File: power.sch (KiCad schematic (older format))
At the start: 46 parts, among them J2 BATT_OUT, J3 BATT_IN, J4 Barrel_Jack_Switch, K1 UMS05-1A80-75L, Q2 Q_NMOS_DSG, SW2 SW_Reed, U1 TPS62821DLC, U4 TPS62821DLC, U5 P783F-Q24-S5-S

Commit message: Small fixes to schematic.
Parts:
- added R?: 39k, symbol Device:R_US
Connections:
- wire segments 132 -> 133
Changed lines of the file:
@@
 RELAY-
 Wire Wire Line
-	2000 5250 1200 5250
-Wire Wire Line
 	1200 5250 1200 5450
-Connection ~ 2000 5250
 $Comp
 L Device:R_US R10
@@
 Wire Wire Line
 	1200 5250 1050 5250
-Connection ~ 1200 5250
 Wire Notes Line width 20
 	550  4000 3200 4000
@@
 $EndComp
 NoConn ~ 8400 1050
+$Comp
+L Device:R_US R?
+U 1 1 618DE97F
+P 1550 5250
+F 0 "R?" V 1345 5250 50  0000 C CNN
+F 1 "39k" V 1436 5250 50  0000 C CNN
+F 2 "" V 1590 5240 50  0001 C CNN
+F 3 "~" H 1550 5250 50  0001 C CNN
+	1    1550 5250
+	0    1    1    0
+$EndComp
+Wire Wire Line
+	1200 5250 1400 5250
+Connection ~ 1200 5250
+Wire Wire Line
+	1700 5250 2000 5250
+Connection ~ 2000 5250
 $EndSCHEMATC

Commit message: Updated footprints. Placed components and added silkscreen.
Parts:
- removed C26: 0.47u, Capacitor_SMD:C_1206_3216Metric, symbol Device:C
- removed C27, C28: 4.7u, Capacitor_SMD:C_1206_3216Metric, symbol Device:C
- removed C30, C31, C33, C34: 10u, Capacitor_SMD:C_1206_3216Metric, symbol Device:C
- removed L1, L2: 0.47u, Inductor_SMD:L_0603_1608Metric, symbol Device:L
- removed R15: 30k, Resistor_SMD:R_0603_1608Metric, symbol Device:R_US
- removed R16: 20k, Resistor_SMD:R_0603_1608Metric, symbol Device:R_US
- removed R17: 50k, Resistor_SMD:R_0603_1608Metric, symbol Device:R_US
- removed R19: 470k, Resistor_SMD:R_0603_1608Metric, symbol Device:R_US
- removed R20, R22: 100k, Resistor_SMD:R_0603_1608Metric, symbol Device:R_US
- removed R21: 82k, Resistor_SMD:R_0603_1608Metric, symbol Device:R_US
- removed TP10: 3.3v, TestPoint:TestPoint_Pad_1.5x1.5mm, symbol Connector:TestPoint
- removed TP6: 1.1v EN, TestPoint:TestPoint_Pad_1.5x1.5mm, symbol Connector:TestPoint
- removed TP7: 3.3v EN, TestPoint:TestPoint_Pad_1.5x1.5mm, symbol Connector:TestPoint
- removed TP8: 1.1v, TestPoint:TestPoint_Pad_1.5x1.5mm, symbol Connector:TestPoint
- removed U1, U4: TPS62821DLC, Package_DFN_QFN:Texas_VSON-HR-8_1.5x2mm_P0.5mm, symbol Regulator_Switching:TPS62821DLC
- added J11: Screw_Terminal_01x02, TerminalBlock:TerminalBlock_bornier-2_P5.08mm, symbol Connector:Screw_Terminal_01x02
- D2, D3: footprint Diode_SMD:D_0603_1608Metric -> Diode_SMD:D_1206_3216Metric_Pad1.42x1.75mm_HandSolder
- J2: footprint TerminalBlock:TerminalBlock_Altech_AK300-2_P5.00mm -> TerminalBlock:TerminalBlock_bornier-2_P5.08mm
- R1: renamed from R?; footprint (none) -> Resistor_SMD:R_1206_3216Metric_Pad1.30x1.75mm_HandSolder
- R10, R11, R12, R13, R14, R18: footprint Resistor_SMD:R_0603_1608Metric -> Resistor_SMD:R_1206_3216Metric_Pad1.30x1.75mm_HandSolder
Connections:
- net labels removed: +1V1, +3V3
- wire segments 133 -> 70
- no-connect marks 2 -> 1
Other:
- note removed: "RC Filter delays enable by 9.5ms"
- moved on the sheet: C29, C32, D4, D5, F1, J2, J3, J4, K1, R14, R18, TP9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

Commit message: Changed footprints to right angle versions. Adjusted board outline to orbitty carrier size.
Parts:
- J3: footprint Connector_AMASS:AMASS_XT30U-F_1x02_P5.0mm_Vertical -> Connector_AMASS:AMASS_XT30PW-M_1x02_P2.50mm_Horizontal
- SW2: footprint Connector_JST:JST_PH_B2B-PH-K_1x02_P2.00mm_Vertical -> Connector_JST:JST_PH_S2B-PH-K_1x02_P2.00mm_Horizontal
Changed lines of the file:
@@
 F 0 "SW2" V 2046 4965 50  0000 R CNN
 F 1 "SW_Reed" V 1955 4965 50  0000 R CNN
-F 2 "Connector_JST:JST_PH_B2B-PH-K_1x02_P2.00mm_Vertical" H 2000 5050 50  0001 C CNN
+F 2 "Connector_JST:JST_PH_S2B-PH-K_1x02_P2.00mm_Horizontal" H 2000 5050 50  0001 C CNN
 F 3 "~" H 2000 5050 50  0001 C CNN
 	1    2000 5050
@@
 F 0 "J3" H 1180 2242 50  0000 L CNN
 F 1 "BATT_IN" H 1180 2151 50  0000 L CNN
-F 2 "Connector_AMASS:AMASS_XT30U-F_1x02_P5.0mm_Vertical" H 1100 2250 50  0001 C CNN
+F 2 "Connector_AMASS:AMASS_XT30PW-M_1x02_P2.50mm_Horizontal" H 1100 2250 50  0001 C CNN
 F 3 "~" H 1100 2250 50  0001 C CNN
 	1    1100 2250

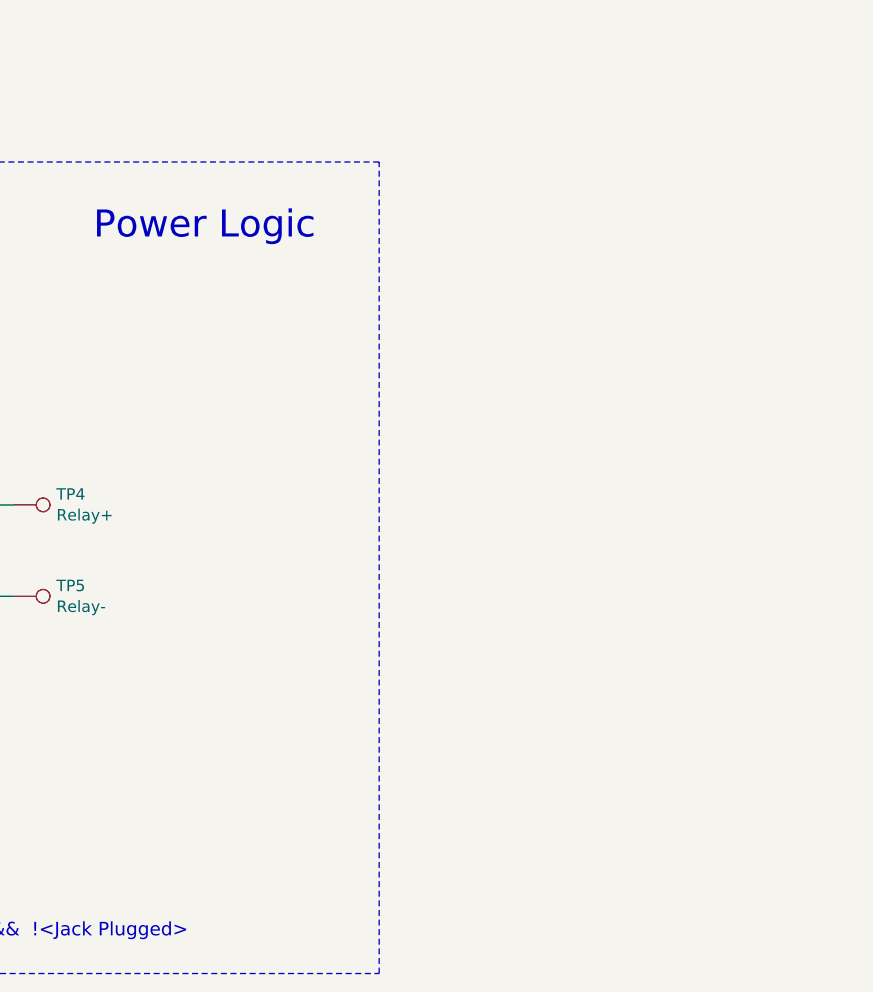
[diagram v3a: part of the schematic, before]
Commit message: Added battery undervoltage protection, needs consideration as to whether it would work.
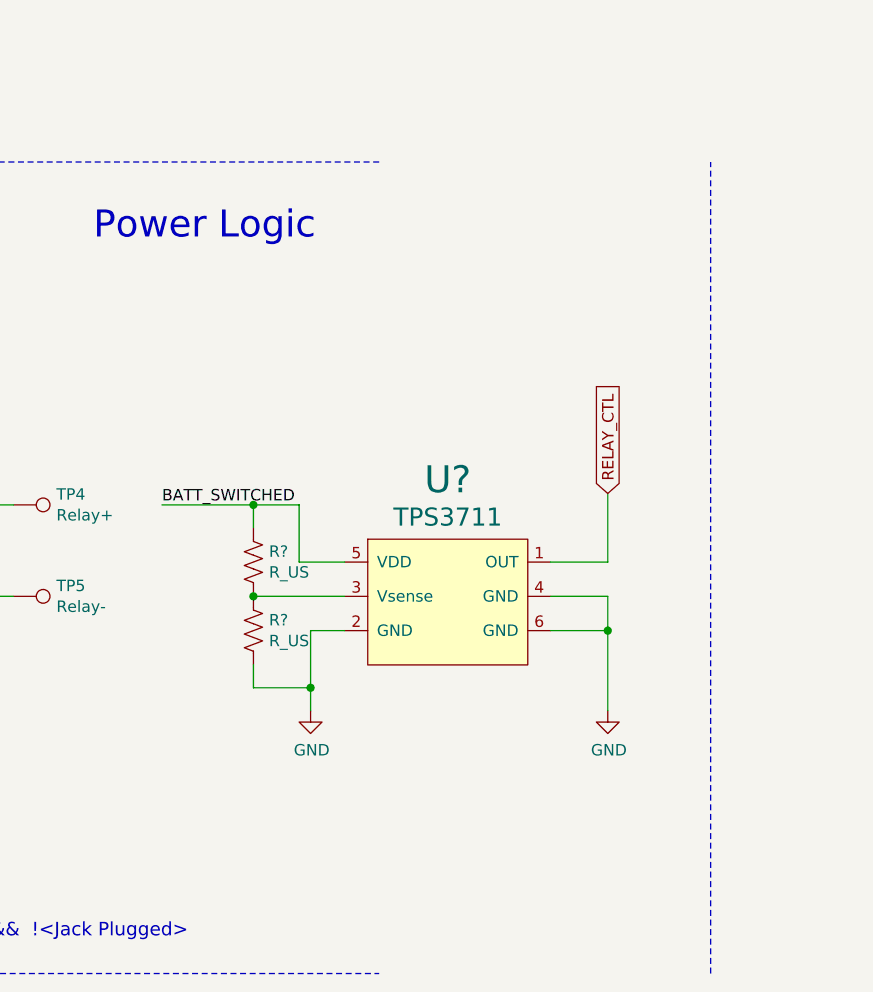
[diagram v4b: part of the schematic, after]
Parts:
- added R? (x2): R_US, symbol Device:R_US
- added U?: TPS3711, symbol New_Library:TPS3711
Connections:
- net BATT_SWITCHED: now also R?.1, U?.5 (VDD)
- net GND: now also R?.2, U?.2 (GND), U?.4 (GND), U?.6 (GND)
- net RELAY_CTL: now also U?.1 (OUT)
- new net: R?.1, R?.2, U?.3 (Vsense)
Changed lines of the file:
@@
 	550  7700 5400 7700
 Wire Notes Line width 20
-	5400 7700 5400 4150
+	6850 7700 6850 4150
 Wire Notes Line width 20
 	5400 4150 550  4150
@@
 	1    0    0    -1
 $EndComp
+$Comp
+L New_Library:TPS3711 U?
+U 1 1 618E2051
+P 5700 6200
+F 0 "U?" H 5700 6860 118 0000 C CNN
+F 1 "TPS3711" H 5700 6696 79  0000 C CNN
+F 2 "" H 5700 6700 118 0001 C CNN
+F 3 "" H 5700 6700 118 0001 C CNN
+	1    5700 6200
+	1    0    0    -1
+$EndComp
+$Comp
+L power:GND #PWR?
+U 1 1 618E412F
+P 6400 6550
+F 0 "#PWR?" H 6400 6300 50  0001 C CNN
+F 1 "GND" H 6405 6377 50  0000 C CNN
+F 2 "" H 6400 6550 50  0001 C CNN
+F 3 "" H 6400 6550 50  0001 C CNN
+	1    6400 6550
+	1    0    0    -1
+$EndComp
+Wire Wire Line
+	6150 6050 6400 6050
+Wire Wire Line
+	6400 6050 6400 6200
+Wire Wire Line
+	6150 6200 6400 6200
+Connection ~ 6400 6200
+Wire Wire Line
+	6400 6200 6400 6550
+Wire Wire Line
+	5250 6200 5100 6200
+Wire Wire Line
+	5100 6200 5100 6450
+$Comp
+L power:GND #PWR?
+U 1 1 618EA162
+P 5100 6550
+F 0 "#PWR?" H 5100 6300 50  0001 C CNN
+F 1 "GND" H 5105 6377 50  0000 C CNN
+F 2 "" H 5100 6550 50  0001 C CNN
+F 3 "" H 5100 6550 50  0001 C CNN
+	1    5100 6550
+	1    0    0    -1
+$EndComp
+Wire Wire Line
+	6150 5900 6400 5900
+Wire Wire Line
+	6400 5900 6400 5600
+Text GLabel 6400 5600 1    50   Input ~ 0
+RELAY_CTL
+Wire Wire Line
+	5250 5900 5050 5900
+Wire Wire Line
+	5050 5900 5050 5650
+Wire Wire Line
+	5250 6050 4850 6050
+$Comp
+L Device:R_US R?
+U 1 1 618F8E38
+P 4850 5900
+F 0 "R?" H 4918 5946 50  0000 L CNN
+F 1 "R_US" H 4918 5855 50  0000 L CNN
+F 2 "" V 4890 5890 50  0001 C CNN
+F 3 "~" H 4850 5900 50  0001 C CNN
+	1    4850 5900
+	1    0    0    -1
+$EndComp
+$Comp
+L Device:R_US R?
+U 1 1 618F9768
+P 4850 6200
+F 0 "R?" H 4918 6246 50  0000 L CNN
+F 1 "R_US" H 4918 6155 50  0000 L CNN
+F 2 "" V 4890 6190 50  0001 C CNN
+F 3 "~" H 4850 6200 50  0001 C CNN
+	1    4850 6200
+	1    0    0    -1
+$EndComp
+Connection ~ 4850 6050
+Wire Wire Line
+	4850 6350 4850 6450
+Wire Wire Line
+	4850 6450 5100 6450
+Connection ~ 5100 6450
+Wire Wire Line
+	5100 6450 5100 6550
+Wire Wire Line
+	4850 5750 4850 5650
+Wire Wire Line
+	4850 5650 5050 5650
+Wire Wire Line
+	4850 5650 4450 5650
+Connection ~ 4850 5650
+Text Label 4450 5650 0    50   ~ 0
+BATT_SWITCHED
 $EndSCHEMATC

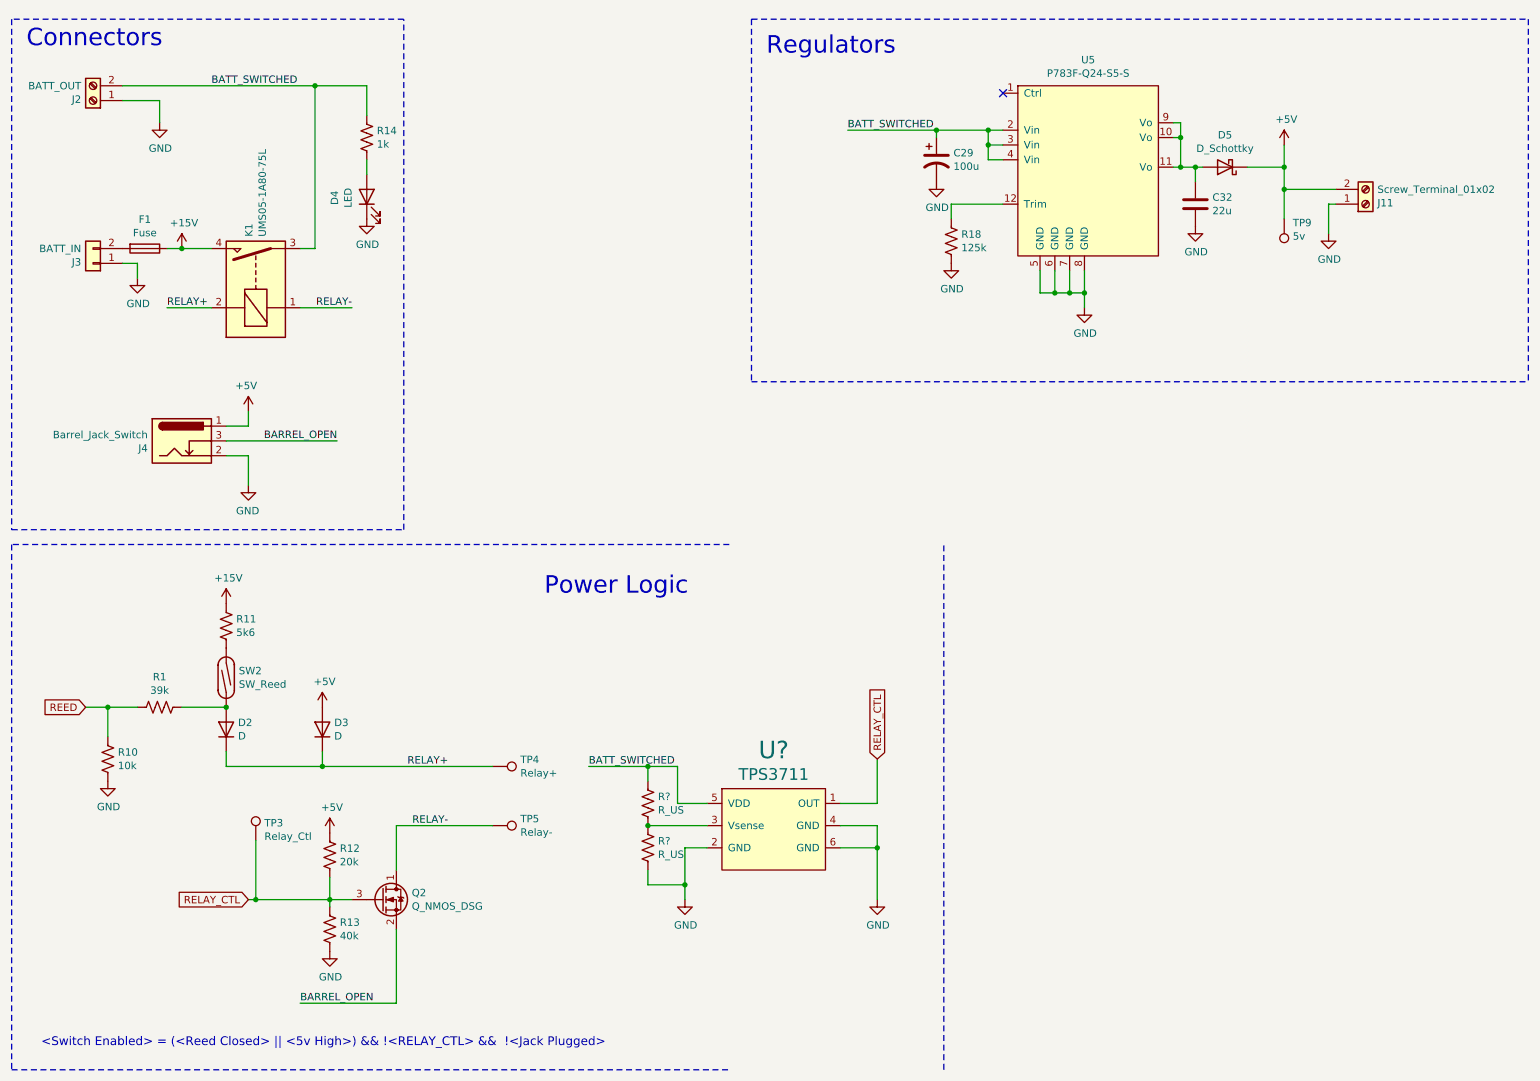
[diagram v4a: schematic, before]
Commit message: Removed uneeded DC barrel power. Adjusted component values for 12v supply. Checked footprints.
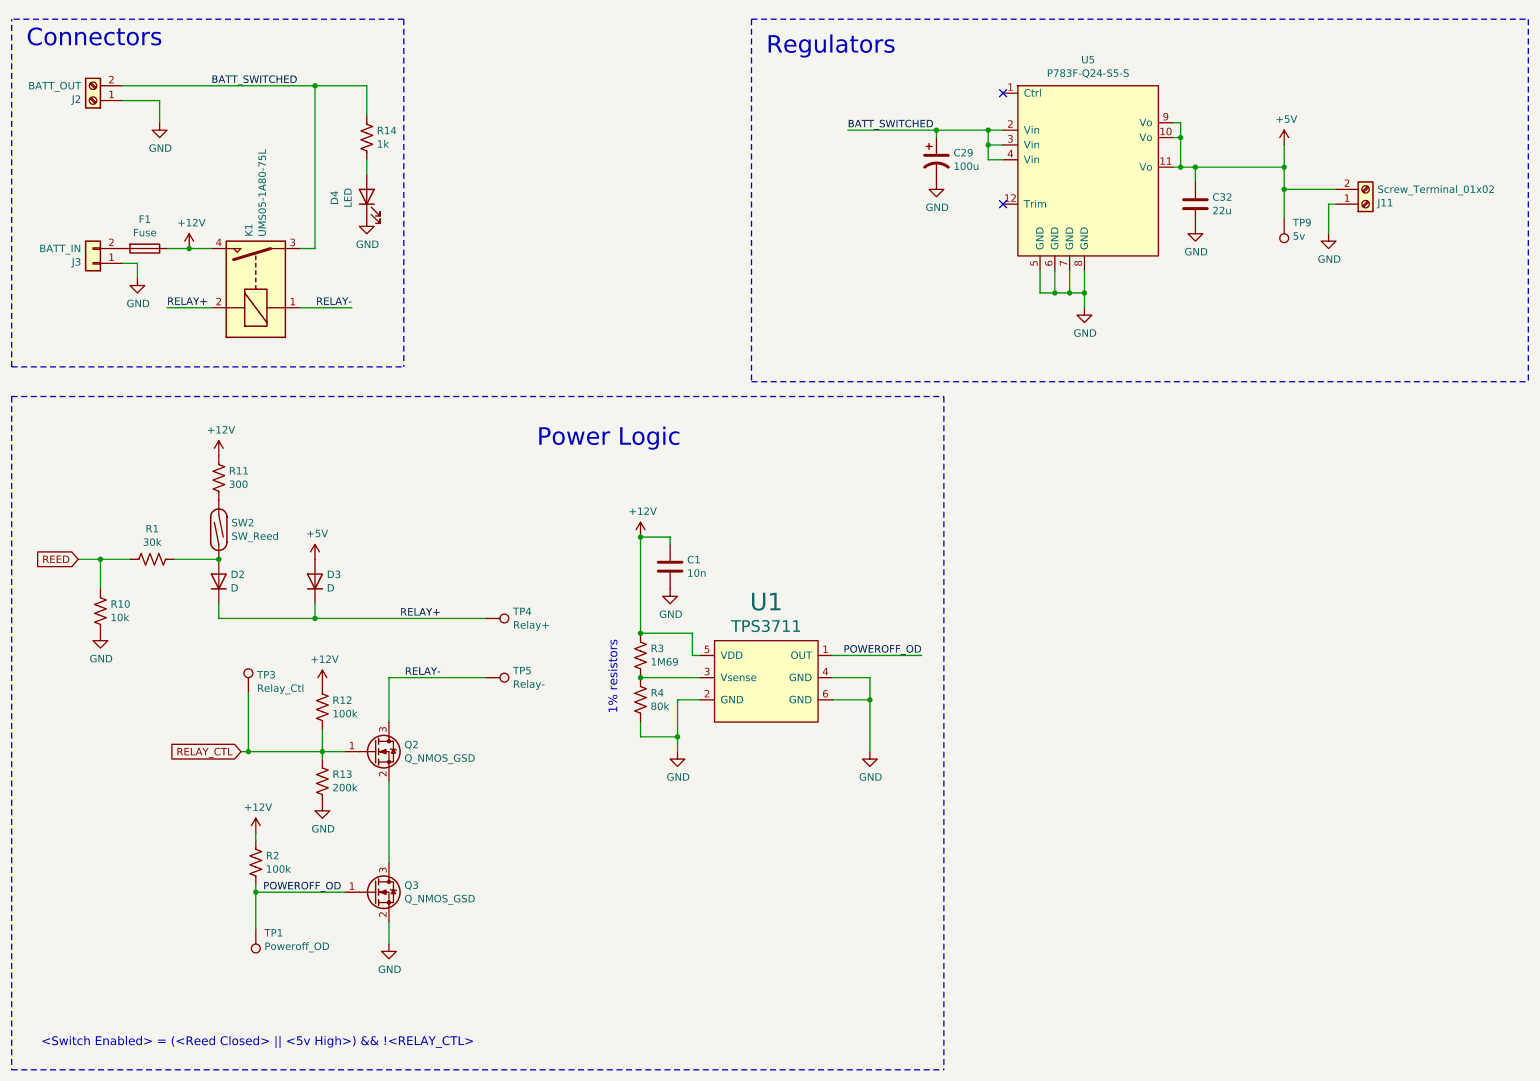
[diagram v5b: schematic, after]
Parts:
- removed D5: D_Schottky, Diode_SMD:D_1206_3216Metric, symbol Device:D_Schottky
- removed J4: Barrel_Jack_Switch, Connector_BarrelJack:BarrelJack_Wuerth_6941xx301002, symbol Connector:Barrel_Jack_Switch
- removed Q2: Q_NMOS_DSG, Package_TO_SOT_SMD:SOT-23, symbol Device:Q_NMOS_DSG
- removed R18: 125k, Resistor_SMD:R_1206_3216Metric_Pad1.30x1.75mm_HandSolder, symbol Device:R_US
- added C1: 10n, Capacitor_SMD:C_1206_3216Metric_Pad1.33x1.80mm_HandSolder, symbol Device:C
- added Q2, Q3: Q_NMOS_GSD, Package_TO_SOT_SMD:SOT-23_Handsoldering, symbol Device:Q_NMOS_GSD
- added R2: 100k, Resistor_SMD:R_1206_3216Metric_Pad1.30x1.75mm_HandSolder, symbol Device:R_US
- added TP1: Poweroff_OD, TestPoint:TestPoint_Pad_1.5x1.5mm, symbol Connector:TestPoint
- R1: value 39k -> 30k
- R11: value 5k6 -> 300
- R12: value 20k -> 100k
- R13: value 40k -> 200k
- R3: renamed from R?; value R_US -> 1M69; footprint (none) -> Resistor_SMD:R_1206_3216Metric_Pad1.30x1.75mm_HandSolder
- R4: renamed from R?; value R_US -> 80k; footprint (none) -> Resistor_SMD:R_1206_3216Metric_Pad1.30x1.75mm_HandSolder
- U1: renamed from U?; footprint (none) -> Package_TO_SOT_SMD:SOT-23-6_Handsoldering
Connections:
- net +5V: now also C32.1, U5.10 (Vo), U5.11 (Vo), U5.9 (Vo); no longer R12.1
- net BATT_SWITCHED: no longer R3.1, U1.5 (VDD)
- net GND: now also C1.2, Q3.2 (S)
- net RELAY-: now also Q2.3 (D)
- net RELAY_CTL: now also Q2.1 (G); no longer U1.1 (OUT)
- net +15V renamed +12V
- net +12V: now also R12.1, R3.1, U1.5 (VDD), C1.1, R2.1
- new net: Q2.2 (S), Q3.3 (D)
- new net POWEROFF_OD: Q3.1 (G), R2.2, TP1.1, U1.1 (OUT)
- no-connect marks 1 -> 2
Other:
- note added: "1% resistors\n"
- note added: "<Switch Enabled> = (<Reed Closed> || <5v High>) && !<RELAY_CTL>"
- note removed: "<Switch Enabled> = (<Reed Closed> || <5v High>) && !<RELAY_CTL> && !<Jack Plugged>"
- moved on the sheet: D2, D3, R1, R10, R11, R12, R13, R3, R4, SW2, TP3, TP4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
